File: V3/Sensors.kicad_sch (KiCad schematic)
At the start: 13 parts, among them U1 L80-M39, U2 MS561101BA03-50, U3 ADXL375BCCZ-RL7

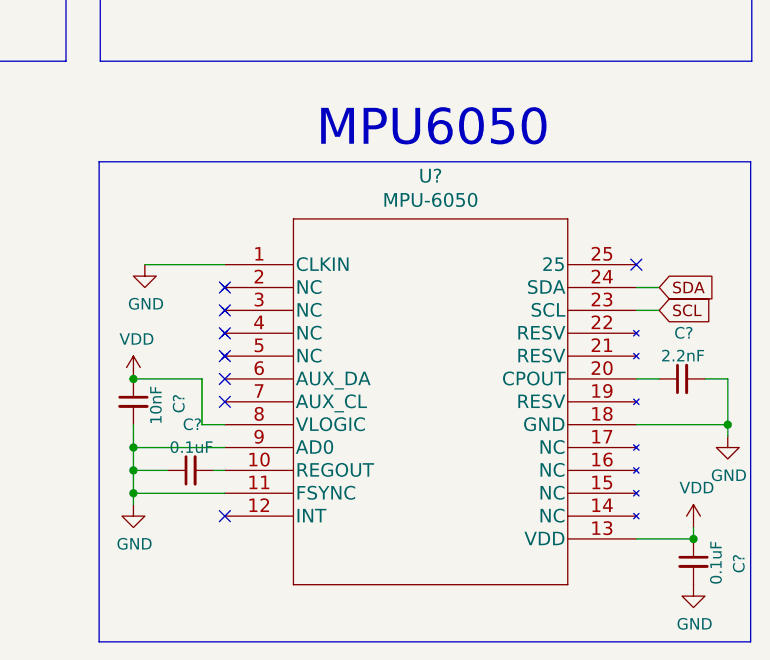
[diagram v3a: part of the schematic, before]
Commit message: almost finished component placement
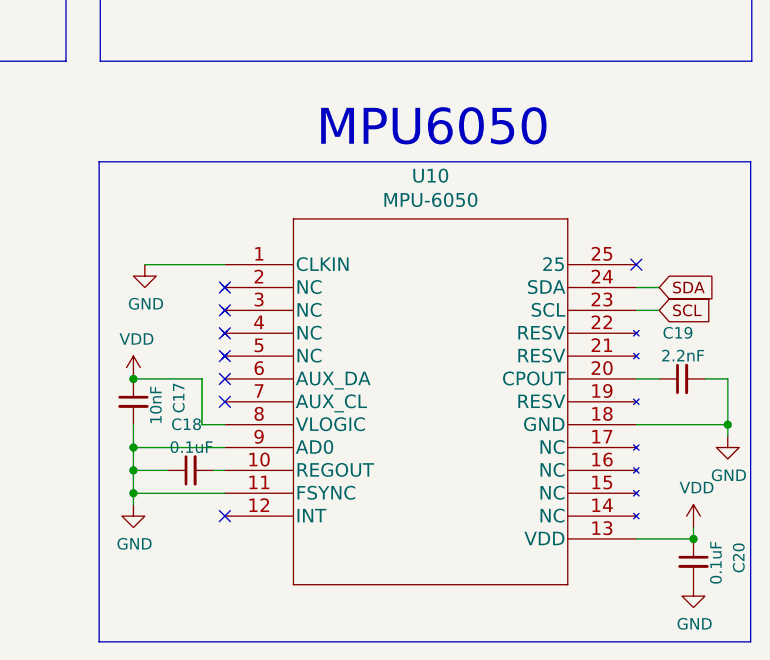
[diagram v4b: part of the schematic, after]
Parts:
- gave numbers to parts that had none: 5
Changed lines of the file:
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@@
   (symbol (lib_id "Device:C_Small") (at 149.098 130.556 0) (unit 1)
     (in_bom yes) (on_board yes)
-    (property "Reference" "C?" (id 0) (at 154.178 131.826 90)
+    (property "Reference" "C17" (id 0) (at 154.178 131.826 90)
       (effects (font (size 1.27 1.27)) (justify left))
     )
@@
   (symbol (lib_id "power:GND") (at 211.328 150.876 0) (unit 1)
     (in_bom yes) (on_board yes)
-    (property "Reference" "#PWR?" (id 0) (at 211.328 157.226 0)
+    (property "Reference" "#PWR0171" (id 0) (at 211.328 157.226 0)
       (effects (font (size 1.27 1.27)) hide)
     )
@@
   (symbol (lib_id "power:GND") (at 149.098 141.986 0) (unit 1)
     (in_bom yes) (on_board yes)
-    (property "Reference" "#PWR?" (id 0) (at 149.098 148.336 0)
+    (property "Reference" "#PWR0172" (id 0) (at 149.098 148.336 0)
       (effects (font (size 1.27 1.27)) hide)
     )
@@
   (symbol (lib_id "power:GND") (at 150.368 115.316 0) (unit 1)
     (in_bom yes) (on_board yes)
-    (property "Reference" "#PWR?" (id 0) (at 150.368 121.666 0)
+    (property "Reference" "#PWR0144" (id 0) (at 150.368 121.666 0)
       (effects (font (size 1.27 1.27)) hide)
     )
@@
   (symbol (lib_id "Device:C_Small") (at 155.448 138.176 90) (unit 1)
     (in_bom yes) (on_board yes)
-    (property "Reference" "C?" (id 0) (at 156.718 133.096 90)
+    (property "Reference" "C18" (id 0) (at 156.718 133.096 90)
       (effects (font (size 1.27 1.27)) (justify left))
     )
@@
   (symbol (lib_id "power:VDD") (at 148.082 58.42 0) (unit 1)
     (in_bom yes) (on_board yes)
-    (property "Reference" "#PWR?" (id 0) (at 148.082 62.23 0)
+    (property "Reference" "#PWR0167" (id 0) (at 148.082 62.23 0)
       (effects (font (size 1.27 1.27)) hide)
     )
@@
   (symbol (lib_id "MPU-6050:MPU-6050") (at 159.258 115.316 0) (unit 1)
     (in_bom yes) (on_board yes)
-    (property "Reference" "U?" (id 0) (at 182.118 105.4862 0)
+    (property "Reference" "U10" (id 0) (at 182.118 105.4862 0)
       (effects (font (size 1.524 1.524)))
     )
@@
   (symbol (lib_id "power:VDD") (at 211.328 144.526 0) (unit 1)
     (in_bom yes) (on_board yes)
-    (property "Reference" "#PWR?" (id 0) (at 211.328 148.336 0)
+    (property "Reference" "#PWR0169" (id 0) (at 211.328 148.336 0)
       (effects (font (size 1.27 1.27)) hide)
     )
@@
   (symbol (lib_id "power:VDD") (at 149.098 128.016 0) (unit 1)
     (in_bom yes) (on_board yes)
-    (property "Reference" "#PWR?" (id 0) (at 149.098 131.826 0)
+    (property "Reference" "#PWR0145" (id 0) (at 149.098 131.826 0)
       (effects (font (size 1.27 1.27)) hide)
     )
@@
   (symbol (lib_id "power:GND") (at 215.138 134.366 0) (unit 1)
     (in_bom yes) (on_board yes)
-    (property "Reference" "#PWR?" (id 0) (at 215.138 140.716 0)
+    (property "Reference" "#PWR0170" (id 0) (at 215.138 140.716 0)
       (effects (font (size 1.27 1.27)) hide)
     )
@@
   (symbol (lib_id "Device:C_Small") (at 211.328 148.336 0) (unit 1)
     (in_bom yes) (on_board yes)
-    (property "Reference" "C?" (id 0) (at 216.408 149.606 90)
+    (property "Reference" "C20" (id 0) (at 216.408 149.606 90)
       (effects (font (size 1.27 1.27)) (justify left))
     )
@@
   (symbol (lib_id "power:VDD") (at 148.082 80.01 0) (unit 1)
     (in_bom yes) (on_board yes)
-    (property "Reference" "#PWR?" (id 0) (at 148.082 83.82 0)
+    (property "Reference" "#PWR0168" (id 0) (at 148.082 83.82 0)
       (effects (font (size 1.27 1.27)) hide)
     )
@@
   (symbol (lib_id "Device:C_Small") (at 210.058 128.016 90) (unit 1)
     (in_bom yes) (on_board yes)
-    (property "Reference" "C?" (id 0) (at 211.328 122.936 90)
+    (property "Reference" "C19" (id 0) (at 211.328 122.936 90)
       (effects (font (size 1.27 1.27)) (justify left))
     )
@@
   (symbol (lib_id "power:GND") (at 211.582 64.262 0) (unit 1)
     (in_bom yes) (on_board yes)
-    (property "Reference" "#PWR?" (id 0) (at 211.582 70.612 0)
-      (effects (font (size 1.27 1.27)) hide)
-    )
+    (property "Reference" "#PWR0166" (id 0) (at 211.582 70.612 0)
+      (effects (font (size 1.27 1.27)) hide)
+    )

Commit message: Updated costing sheet:
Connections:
- net GND: now also U10.25
- no-connect marks 17 -> 16
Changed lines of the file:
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@@
   (junction (at 55.88 131.445) (diameter 0) (color 0 0 0 0)
+  )
+  (junction (at 215.265 115.443) (diameter 0) (color 0 0 0 0)
   )
   (junction (at 149.098 135.636) (diameter 0) (color 0 0 0 0)
@@
   (no_connect (at 159.258 117.856))
   (no_connect (at 159.258 125.476))
-  (no_connect (at 204.978 115.316))
   (no_connect (at 204.724 66.04))
   (no_connect (at 204.724 73.66))
@@
     (stroke (width 0) (type default) (color 0 0 0 0))
   )
+  (wire (pts (xy 215.265 115.316) (xy 215.265 115.443))
+    (stroke (width 0) (type default) (color 0 0 0 0))
+  )
   (wire (pts (xy 204.978 133.096) (xy 215.138 133.096))
     (stroke (width 0) (type default) (color 0 0 0 0))
@@
   )
   (wire (pts (xy 156.718 128.016) (xy 149.098 128.016))
+    (stroke (width 0) (type default) (color 0 0 0 0))
+  )
+  (wire (pts (xy 204.978 115.316) (xy 215.265 115.316))
     (stroke (width 0) (type default) (color 0 0 0 0))
   )
@@
     (pin "2")
   )
+  (symbol (lib_id "power:GND") (at 215.265 115.443 0) (unit 1)
+    (in_bom yes) (on_board yes)
+    (property "Reference" "#PWR0142" (id 0) (at 215.265 121.793 0)
+      (effects (font (size 1.27 1.27)) hide)
+    )
+    (property "Value" "GND" (id 1) (at 215.392 119.8372 0))
+    (property "Footprint" "" (id 2) (at 215.265 115.443 0)
+      (effects (font (size 1.27 1.27)) hide)
+    )
+    (property "Datasheet" "" (id 3) (at 215.265 115.443 0)
+      (effects (font (size 1.27 1.27)) hide)
+    )
+    (pin "1")
+  )
   (symbol (lib_id "power:GND") (at 211.328 150.876 0) (unit 1)

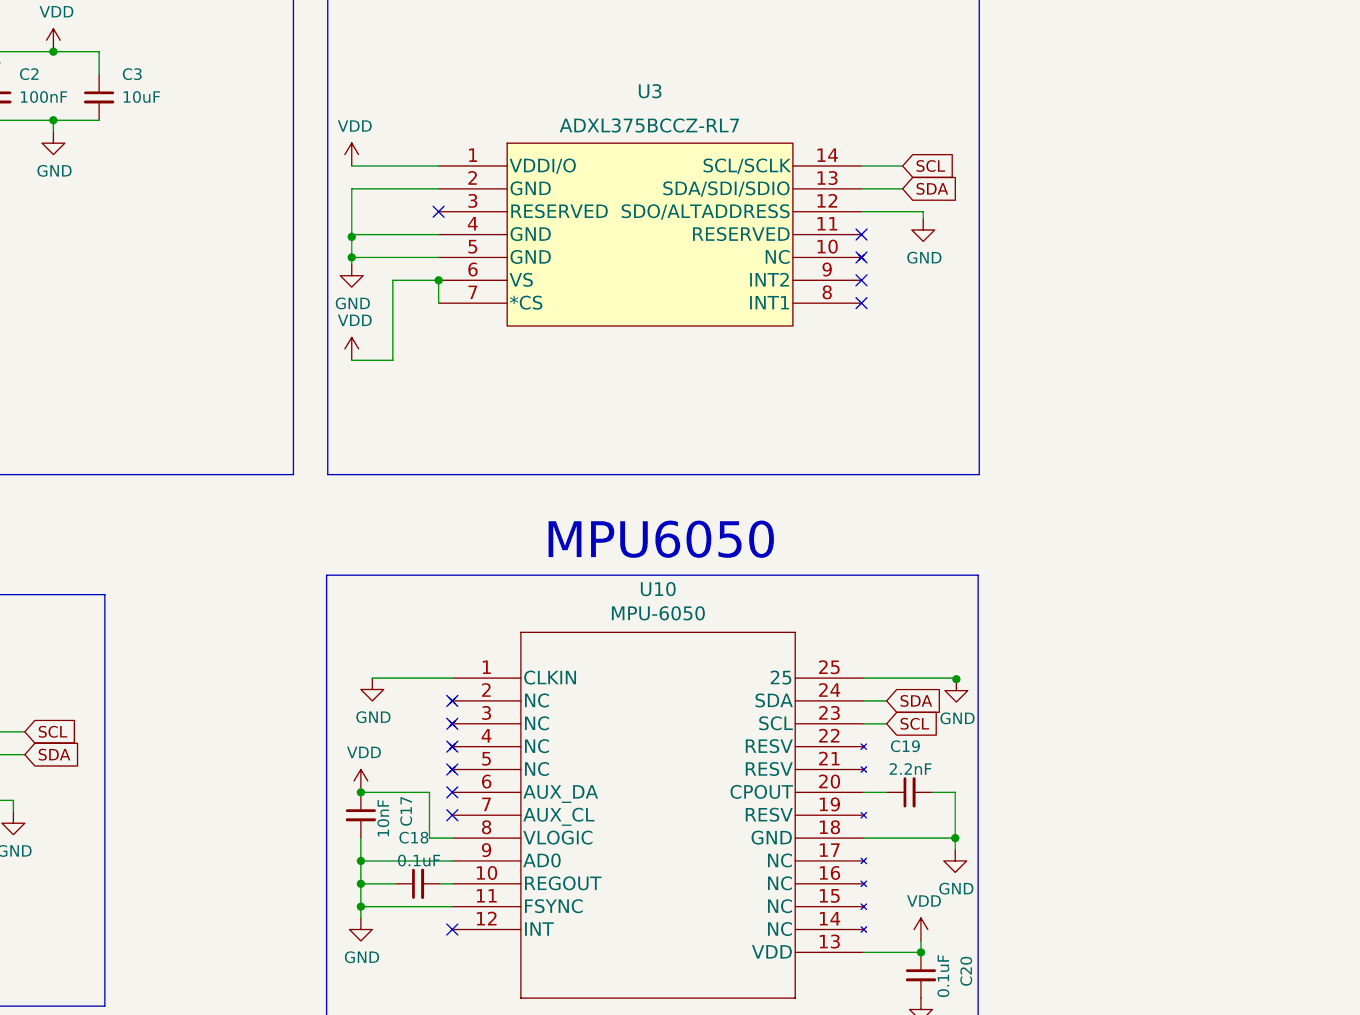
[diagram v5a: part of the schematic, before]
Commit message: Added comments for req changes
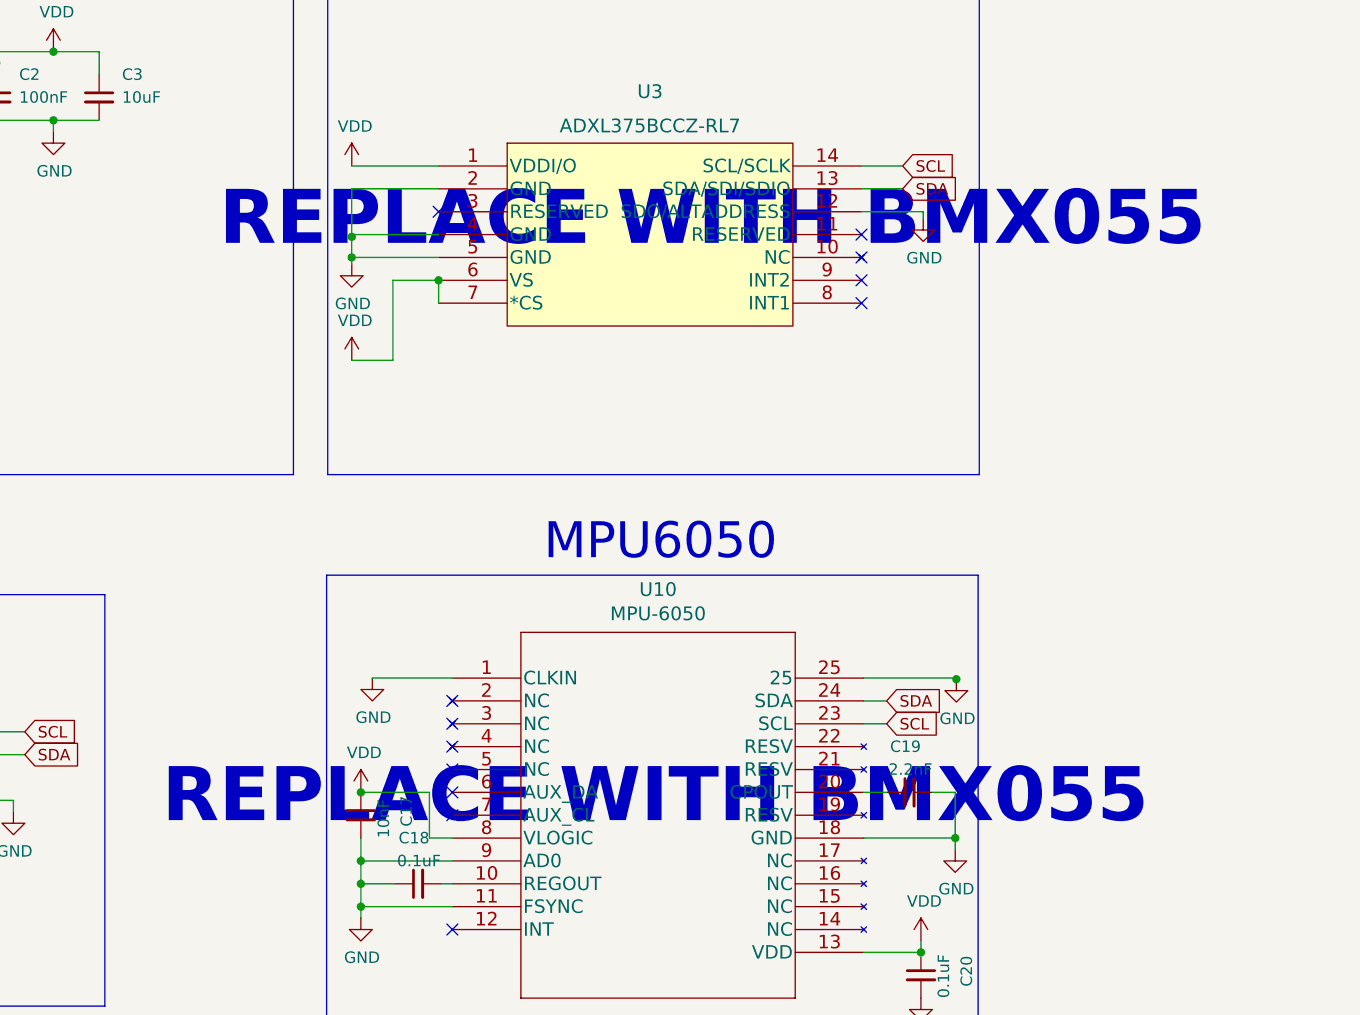
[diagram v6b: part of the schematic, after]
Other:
- note added: "REPLACE WITH BMX055"
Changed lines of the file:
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@@
     (effects (font (size 3.9878 3.9878)) (justify left bottom))
+  )
+  (text "REPLACE WITH BMX055" (at 127 132.08 0)
+    (effects (font (size 6 6) (thickness 1.2) bold) (justify left bottom))
+  )
+  (text "REPLACE WITH BMX055" (at 133.35 67.945 0)
+    (effects (font (size 6 6) (thickness 1.2) bold) (justify left bottom))
   )
   (text "GPS - L80 M39  " (at 70.485 38.1 0)

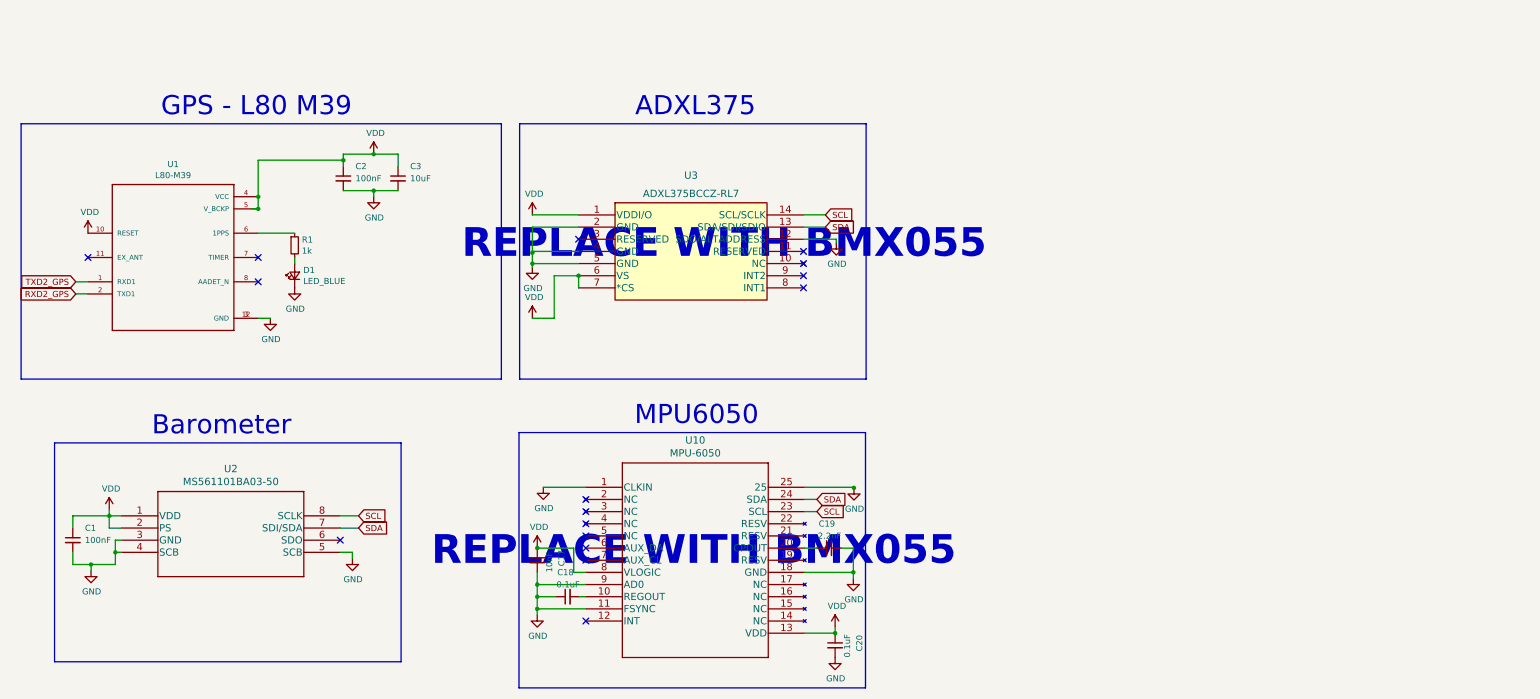
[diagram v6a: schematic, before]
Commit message: New parts placed and routed
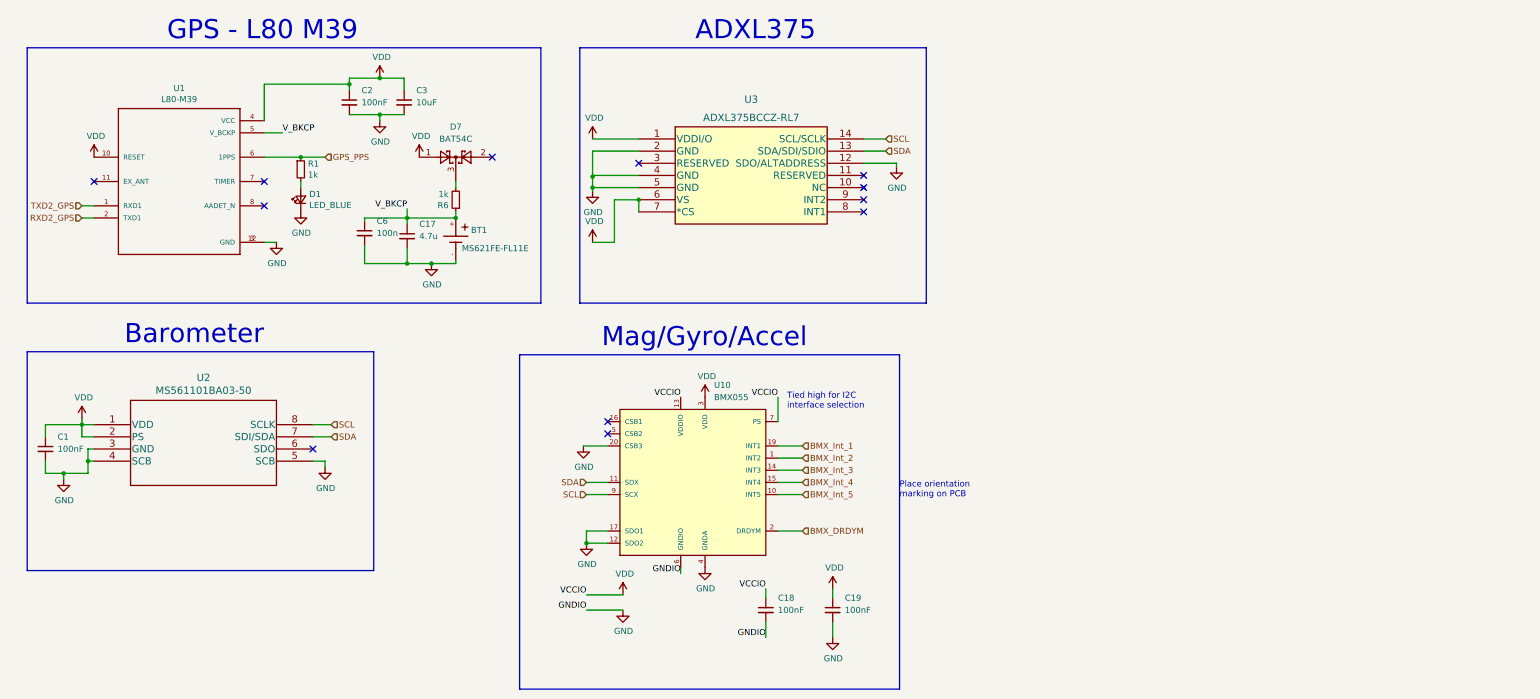
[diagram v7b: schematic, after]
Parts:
- removed C20: 0.1uF, Capacitor_SMD:C_0603_1608Metric, symbol Device:C_Small
- removed U10: MPU-6050, Local_footprints:MPU-6050, symbol MPU-6050:MPU-6050
- added BT1: MS621FE-FL11E, Local_footprints:BAT_MS621FE-FL11E, symbol MS621FE-FL11E:MS621FE-FL11E
- added C6: 100n, Capacitor_SMD:C_0603_1608Metric, symbol Device:C_Small
- added D7: BAT54C, Package_TO_SOT_SMD:SOT-23, symbol Diode:BAT54C
- added R6: 1k, Resistor_SMD:R_0603_1608Metric, symbol Device:R_Small
- added U10: BMX055, Local_footprints:BMX055, symbol BMX055:BMX055
- C17: value 10nF -> 4.7u
- C18: value 0.1uF -> 100nF
- C19: value 2.2nF -> 100nF
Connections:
- net GND: now also C18.2, BT1.-, C6.2, U10.12 (SDO2), U10.17 (SDO1), U10.20 (CSB3), U10.4 (GNDA), U10.6 (GNDIO); no longer C18.1
- net SCL: now also U10.9 (SCX)
- net SDA: now also U10.11 (SDX)
- net VDD: now also C18.1, C19.1, D7.1, U10.13 (VDDIO), U10.3 (VDD), U10.7 (PS); no longer C17.1, U1.5 (V_BCKP)
- net GPS_PPS: now reaches R1.1, U1.6 (1PPS)
- new net: D7.3, R6.2
- new net BMX_DRDYM: U10.2 (DRDYM)
- new net BMX_Int_1: U10.19 (INT1)
- new net BMX_Int_2: U10.1 (INT2)
- new net BMX_Int_3: U10.14 (INT3)
- new net BMX_Int_4: U10.15 (INT4)
- new net BMX_Int_5: U10.10 (INT5)
- new net V_BKCP: BT1.+ (r~), C17.1, C6.1, R6.1, U1.5 (V_BCKP)
- no-connect marks 16 -> 12
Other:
- note added: "Mag/Gyro/Accel"
- note added: "Place orientation marking on PCB"
- note added: "Tied high for I2C interface selection"
- note removed: "MPU6050"
- note removed: "REPLACE WITH BMX055"
- moved on the sheet: C1, C2, C3, D1, R1, U1, U2, U3
